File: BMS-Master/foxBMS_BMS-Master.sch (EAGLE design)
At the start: 314 parts, among them IC1001 AQV252G2S, IC1002 AQV252G2S, IC1003 AQV252G2S, IC1004 AQV252G2S, IC1005 AQV252G2S, IC1006 AQV252G2S, IC1101 UA78L05ACPK, IC1102 ADUM1300ARW, IC1103 ADUM1300ARW, IC1401 IP4220CZ6, IC1402 FT231XS-R, IC1403 ADUM1401ARW, IC1404 IP4220CZ6, IC1405 FT231XS-R, IC1406 ADUM1401ARW, IC1501 AT25128B-SSHL-T, IC1801 IS42S16400J-5TL, IC201 LM1085IS-5.0/NOPB, IC202 MURATA_NCS6S1205C, IC301 LM1085IS-5.0/NOPB, IC302 RS-2405D/H2, IC401 ADR3425ARJZ, IC402 STM32F429IIT6, IC501 STM32F429VIT6, IC601 ADUM1401ARW, IC701 UA78L05ACPK, IC702 ADUM1301ARW, IC801 KA7805ERTF, IC802 TJA1052IT/1Y, IC803 CPC1008N, IC901 LM317MBSTT3G, IC902 CPC1008N, IC903 CPC1008N, IC904 CPC1008N, IC905 CPC1008N, Q401 7B-8.000MAAJ-T, Q501 7B-8.000MAAJ-T, T1001 IRLML0100TRPBF, T1002 IRLML0100TRPBF, T1003 IRLML0100TRPBF, T1004 IRLML0100TRPBF, T1005 IRLML0100TRPBF, T1006 IRLML0100TRPBF, T201 TISP40XXH1BJ, T401 BSS84P, T501 BSS84P, T701 IRLML0100TRPBF, T801 IRLML0100TRPBF, T901 BUK964R8-60E, T902 IRLML0100TRPBF, T903 IRLML0100TRPBF, X1201 43045-0400_MOLEX_4PIN, X1202 43045-0400_MOLEX_4PIN, X1203 43045-0400_MOLEX_4PIN, X1204 43045-0400_MOLEX_4PIN, X1205 43045-0400_MOLEX_4PIN, X1206 43045-0400_MOLEX_4PIN, X1401 MINI-USB-2.0, X1402 MINI-USB-2.0, X1601 43045-1600_MOLEX_16PIN, X201 43045-0600_MOLEX_6PIN, X402 MA02-1, X403 SAMTEC_FTS_20POL_HEADER_VERTI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, X501 MA02-1, X502 SAMTEC_FTS_20POL_HEADER_VERTI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, X701 43045-0400_MOLEX_4PIN, X801 43045-0400_MOLEX_4PIN, X901 43045-0200_MOLEX_2PIN, X902 MA02-1SMALL_PINS_OUTLINE

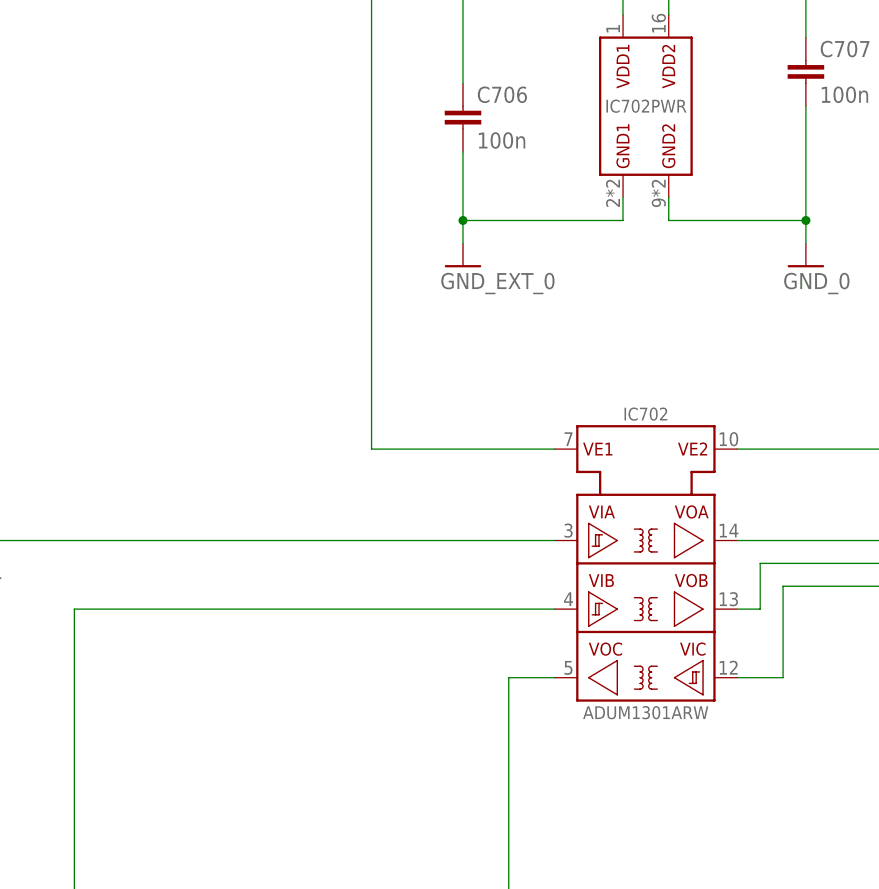
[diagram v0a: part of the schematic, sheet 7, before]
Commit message: Changed ADUM1xxx to ADUM3xxx in schematic of BMS-Master and BMS-Extension
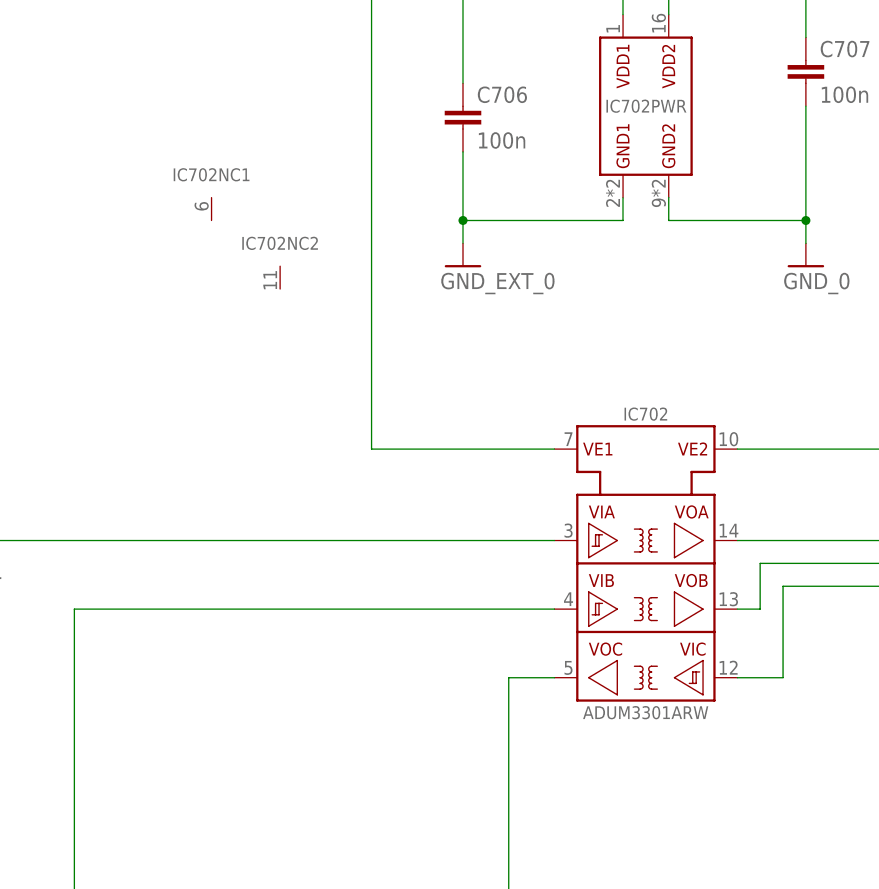
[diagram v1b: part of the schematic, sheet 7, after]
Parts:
- IC1102, IC1103: value ADUM1300ARW -> ADUM3300ARW; device 0_LES_SCHNITTSTELLEN-IC.SMD.ISOLATOR:ADUM1300ARW -> foxBMS_BMS-Master:ADUM3300ARW
- IC1403, IC1406, IC601: value ADUM1401ARW -> ADUM3401ARW; device foxBMS_BMS-Master:ADUM1401ARW -> foxBMS_BMS-Master:ADUM3401ARW
- IC702: value ADUM1301ARW -> ADUM3301ARW; device 0_LES_SCHNITTSTELLEN-IC.SMD.ISOLATOR:ADUM1301ARW -> foxBMS_BMS-Master:ADUM3301ARW
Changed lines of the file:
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@@
 <attributes>
 <attribute name="AUTHOR" value="Fraunhofer IISB foxBMS Team"/>
-<attribute name="REL-DATE" value="2017-05-09"/>
+<attribute name="REL-DATE" value="2017-05-16"/>
 <attribute name="TITLE" value="foxBMS BMS-Master"/>
-<attribute name="VERSION" value="1.0.1"/>
+<attribute name="VERSION" value="1.0.2"/>
 </attributes>
 <variantdefs>
@@
 <part name="X902" library="foxBMS_BMS-Master" deviceset="MA02-1" device="SMALL_PINS_OUTLINE" value="MA02-1SMALL_PINS_OUTLINE"/>
 <part name="IC401" library="foxBMS_BMS-Master" deviceset="ADR34*" device="" technology="25ARJZ"/>
-<part name="IC601" library="foxBMS_BMS-Master" deviceset="ADUM1401" device="" technology="ARW"/>
+<part name="IC601" library="foxBMS_BMS-Master" deviceset="ADUM3401" device="" technology="ARW"/>
 <part name="IC701" library="foxBMS_BMS-Master" deviceset="UA78L*?" device="PK" technology="05AC"/>
-<part name="IC702" library="0_LES_SCHNITTSTELLEN-IC.SMD.ISOLATOR" deviceset="ADUM1301" device="" technology="ARW"/>
+<part name="IC702" library="foxBMS_BMS-Master" deviceset="ADUM3301" device="" technology="ARW"/>
 <part name="IC801" library="foxBMS_BMS-Master" deviceset="KA78*E" device="RTF" technology="05"/>
 <part name="L801" library="foxBMS_BMS-Master" deviceset="B82789" device="" technology="C0513H001"/>
@@
 <part name="IC904" library="foxBMS_BMS-Master" deviceset="CPC1008N" device=""/>
 <part name="IC1101" library="foxBMS_BMS-Master" deviceset="UA78L*?" device="PK" technology="05AC"/>
-<part name="IC1102" library="0_LES_SCHNITTSTELLEN-IC.SMD.ISOLATOR" deviceset="ADUM1300" device="" technology="ARW"/>
-<part name="IC1103" library="0_LES_SCHNITTSTELLEN-IC.SMD.ISOLATOR" deviceset="ADUM1300" device="" technology="ARW"/>
+<part name="IC1102" library="foxBMS_BMS-Master" deviceset="ADUM3300" device="" technology="ARW"/>
+<part name="IC1103" library="foxBMS_BMS-Master" deviceset="ADUM3300" device="" technology="ARW"/>
 <part name="IC1401" library="foxBMS_BMS-Master" deviceset="IP4220CZ6" device=""/>
 <part name="IC1404" library="foxBMS_BMS-Master" deviceset="IP4220CZ6" device=""/>
-<part name="IC1403" library="foxBMS_BMS-Master" deviceset="ADUM1401" device="" technology="ARW"/>
-<part name="IC1406" library="foxBMS_BMS-Master" deviceset="ADUM1401" device="" technology="ARW"/>
+<part name="IC1403" library="foxBMS_BMS-Master" deviceset="ADUM3401" device="" technology="ARW"/>
+<part name="IC1406" library="foxBMS_BMS-Master" deviceset="ADUM3401" device="" technology="ARW"/>
 <part name="IC1501" library="foxBMS_BMS-Master" deviceset="AT25*B-?" device="SSHL-T" technology="128"/>
 <part name="IC1801" library="foxBMS_BMS-Master" deviceset="IS4*S16400J-" device="5TL" technology="2"/>
@@
 <instance part="FRAME6" gate="G$1" x="0" y="0"/>
 <instance part="FRAME6" gate="G$2" x="307.34" y="2.54"/>
+<instance part="IC702" gate="NC1" x="213.36" y="210.82"/>
+<instance part="IC702" gate="NC2" x="220.98" y="203.2"/>
 </instances>
 <busses>

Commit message: updated foxBMS-slave to version 2.02
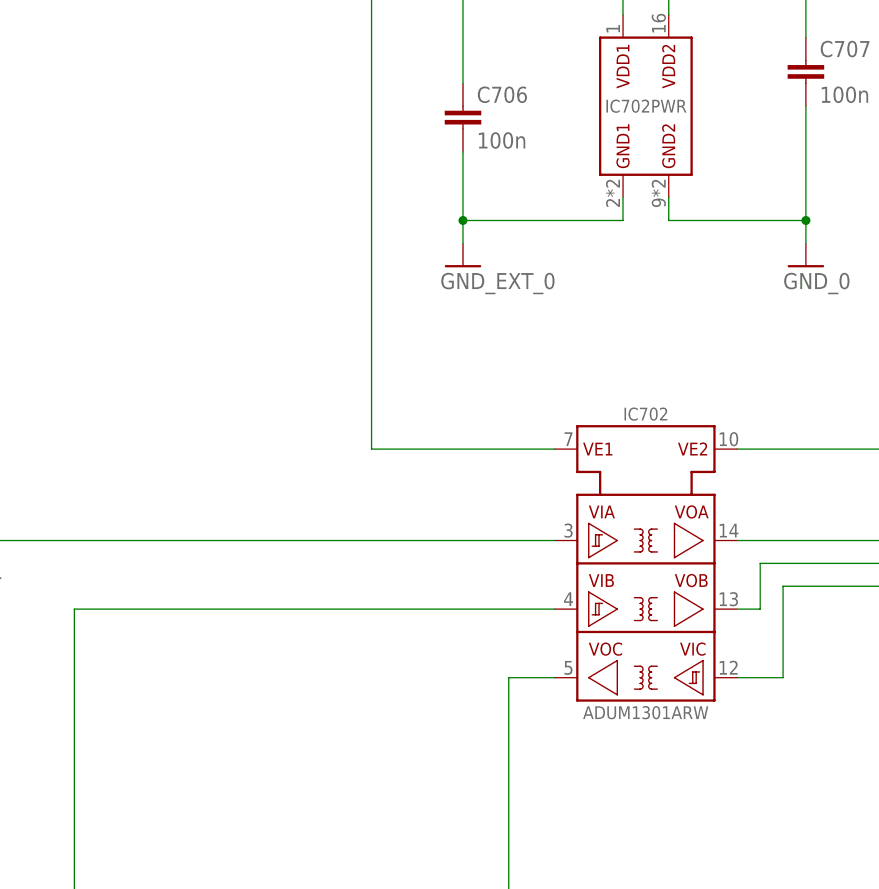
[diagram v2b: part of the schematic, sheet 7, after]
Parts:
- IC1102, IC1103: value ADUM3300ARW -> ADUM1300ARW; device foxBMS_BMS-Master:ADUM3300ARW -> 0_LES_SCHNITTSTELLEN-IC.SMD.ISOLATOR:ADUM1300ARW
- IC1403, IC1406, IC601: value ADUM3401ARW -> ADUM1401ARW; device foxBMS_BMS-Master:ADUM3401ARW -> foxBMS_BMS-Master:ADUM1401ARW
- IC702: value ADUM3301ARW -> ADUM1301ARW; device foxBMS_BMS-Master:ADUM3301ARW -> 0_LES_SCHNITTSTELLEN-IC.SMD.ISOLATOR:ADUM1301ARW
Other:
- note added: "Connectors to Extension Board"
- note added: "Please Note: As the BMS-Master was designed as one unit, the schematic of BMS-Master Basic or Extension may include blank pages."
- note removed: "Connectors to BMS-Extension"
- note removed: "This page was intentionally left blank."
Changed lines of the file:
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@@
 <attributes>
 <attribute name="AUTHOR" value="Fraunhofer IISB foxBMS Team"/>
-<attribute name="REL-DATE" value="2017-05-16"/>
-<attribute name="TITLE" value="foxBMS BMS-Master"/>
-<attribute name="VERSION" value="1.0.2"/>
+<attribute name="REL-DATE" value="2017-04-13"/>
+<attribute name="TITLE" value="foxBMS BMS-Master Basic"/>
+<attribute name="VERSION" value="1.0.1"/>
 </attributes>
 <variantdefs>
@@
 <part name="X902" library="foxBMS_BMS-Master" deviceset="MA02-1" device="SMALL_PINS_OUTLINE" value="MA02-1SMALL_PINS_OUTLINE"/>
 <part name="IC401" library="foxBMS_BMS-Master" deviceset="ADR34*" device="" technology="25ARJZ"/>
-<part name="IC601" library="foxBMS_BMS-Master" deviceset="ADUM3401" device="" technology="ARW"/>
+<part name="IC601" library="foxBMS_BMS-Master" deviceset="ADUM1401" device="" technology="ARW"/>
 <part name="IC701" library="foxBMS_BMS-Master" deviceset="UA78L*?" device="PK" technology="05AC"/>
-<part name="IC702" library="foxBMS_BMS-Master" deviceset="ADUM3301" device="" technology="ARW"/>
+<part name="IC702" library="0_LES_SCHNITTSTELLEN-IC.SMD.ISOLATOR" deviceset="ADUM1301" device="" technology="ARW"/>
 <part name="IC801" library="foxBMS_BMS-Master" deviceset="KA78*E" device="RTF" technology="05"/>
 <part name="L801" library="foxBMS_BMS-Master" deviceset="B82789" device="" technology="C0513H001"/>
@@
 <part name="IC904" library="foxBMS_BMS-Master" deviceset="CPC1008N" device=""/>
 <part name="IC1101" library="foxBMS_BMS-Master" deviceset="UA78L*?" device="PK" technology="05AC"/>
-<part name="IC1102" library="foxBMS_BMS-Master" deviceset="ADUM3300" device="" technology="ARW"/>
-<part name="IC1103" library="foxBMS_BMS-Master" deviceset="ADUM3300" device="" technology="ARW"/>
+<part name="IC1102" library="0_LES_SCHNITTSTELLEN-IC.SMD.ISOLATOR" deviceset="ADUM1300" device="" technology="ARW"/>
+<part name="IC1103" library="0_LES_SCHNITTSTELLEN-IC.SMD.ISOLATOR" deviceset="ADUM1300" device="" technology="ARW"/>
 <part name="IC1401" library="foxBMS_BMS-Master" deviceset="IP4220CZ6" device=""/>
 <part name="IC1404" library="foxBMS_BMS-Master" deviceset="IP4220CZ6" device=""/>
-<part name="IC1403" library="foxBMS_BMS-Master" deviceset="ADUM3401" device="" technology="ARW"/>
-<part name="IC1406" library="foxBMS_BMS-Master" deviceset="ADUM3401" device="" technology="ARW"/>
+<part name="IC1403" library="foxBMS_BMS-Master" deviceset="ADUM1401" device="" technology="ARW"/>
+<part name="IC1406" library="foxBMS_BMS-Master" deviceset="ADUM1401" device="" technology="ARW"/>
 <part name="IC1501" library="foxBMS_BMS-Master" deviceset="AT25*B-?" device="SSHL-T" technology="128"/>
 <part name="IC1801" library="foxBMS_BMS-Master" deviceset="IS4*S16400J-" device="5TL" technology="2"/>
@@
 <wire x1="215.9" y1="238.76" x2="152.4" y2="238.76" width="0.1524" layer="105"/>
 <wire x1="152.4" y1="238.76" x2="152.4" y2="259.08" width="0.1524" layer="105"/>
+<text x="30.48" y="5.08" size="2.54" layer="105">Please Note:
+As the BMS-Master was designed as one unit, the schematic of BMS-Master Basic or Extension may include blank pages.</text>
 </plain>
 <instances>
@@
 <instance part="FRAME6" gate="G$1" x="0" y="0"/>
 <instance part="FRAME6" gate="G$2" x="307.34" y="2.54"/>
-<instance part="IC702" gate="NC1" x="213.36" y="210.82"/>
-<instance part="IC702" gate="NC2" x="220.98" y="203.2"/>
 </instances>
 <busses>
@@
 <plain>
 <text x="335.788" y="24.13" size="2.54" layer="105">Isolated RS485</text>
-<text x="307.34" y="35.56" size="2.54" layer="105">This page was intentionally left blank. </text>
 </plain>
 <instances>
@@
 <plain>
 <text x="336.042" y="24.384" size="2.54" layer="105">Analog Inputs</text>
-<text x="307.34" y="35.56" size="2.54" layer="105">This page was intentionally left blank. </text>
 </plain>
 <instances>
@@
 <plain>
 <text x="336.296" y="24.13" size="2.54" layer="105">Isolated GPIO 4x In /  4x Out</text>
-<text x="307.34" y="35.56" size="2.54" layer="105">This page was intentionally left blank. </text>
 </plain>
 <instances>
@@
 <plain>
 <text x="336.296" y="24.13" size="2.54" layer="105">Isolated Normally Open Contacts</text>
-<text x="307.34" y="35.56" size="2.54" layer="105">This page was intentionally left blank. </text>
 </plain>
 <instances>
@@
 </sheet>
 <sheet>
-<description>Connector BMS-Master to BMS-Extension</description>
+<description>Basic to Extension Connector</description>
 <plain>
-<text x="336.296" y="24.13" size="2.54" layer="105">Connectors to BMS-Extension</text>
+<text x="336.296" y="24.13" size="2.54" layer="105">Connectors to Extension Board</text>
 </plain>
 <instances>
